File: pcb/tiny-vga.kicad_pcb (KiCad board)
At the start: 2 copper layers, 40 x 33 mm, 15 parts, among them J1 PMOD, J2 VGA, U1 74LVC245A

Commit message: Update parts for aisler
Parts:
- removed C1: C, Capacitor_SMD:C_0603_1608Metric_Pad1.08x0.95mm_HandSolder
- removed JP1: SolderJumper_3_Bridged12, Jumper:SolderJumper-3_P1.3mm_Bridged2Bar12_RoundedPad1.0x1.5mm
- RN1, RN2, RN3: footprint Resistor_SMD:R_Array_Convex_4x0402 -> Resistor_SMD:R_Array_Convex_4x0603
- U1: value 74LVC245A -> 74LVC245APW,118
- moved REF** 24.6 mm to (130.5, 64.6)
- moved RN1 0.60 mm to (153.1, 79.3)
- moved RN2 0.60 mm to (153.1, 83.5)
- moved RN3 0.60 mm to (153.1, 87.5)
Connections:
- U1 pad 1: Net-(JP1-C) -> GND
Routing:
- net +3.3V: track 19.8 -> 13.3 mm
- net Net-(JP1-C): track 4.40 -> 0.00 mm
- net GND: track 16.6 -> 15.1 mm, vias 7 -> 6
- net G0: track 6.72 -> 8.03 mm
- net B0: track 8.12 -> 9.20 mm
- net Net-(RN2A-R1.2): track 2.34 -> 3.34 mm
- net Net-(RN1A-R1.2): track 2.56 -> 3.50 mm
- net R0: track 7.11 -> 7.93 mm
- net Net-(RN3A-R1.2): track 2.95 -> 3.48 mm

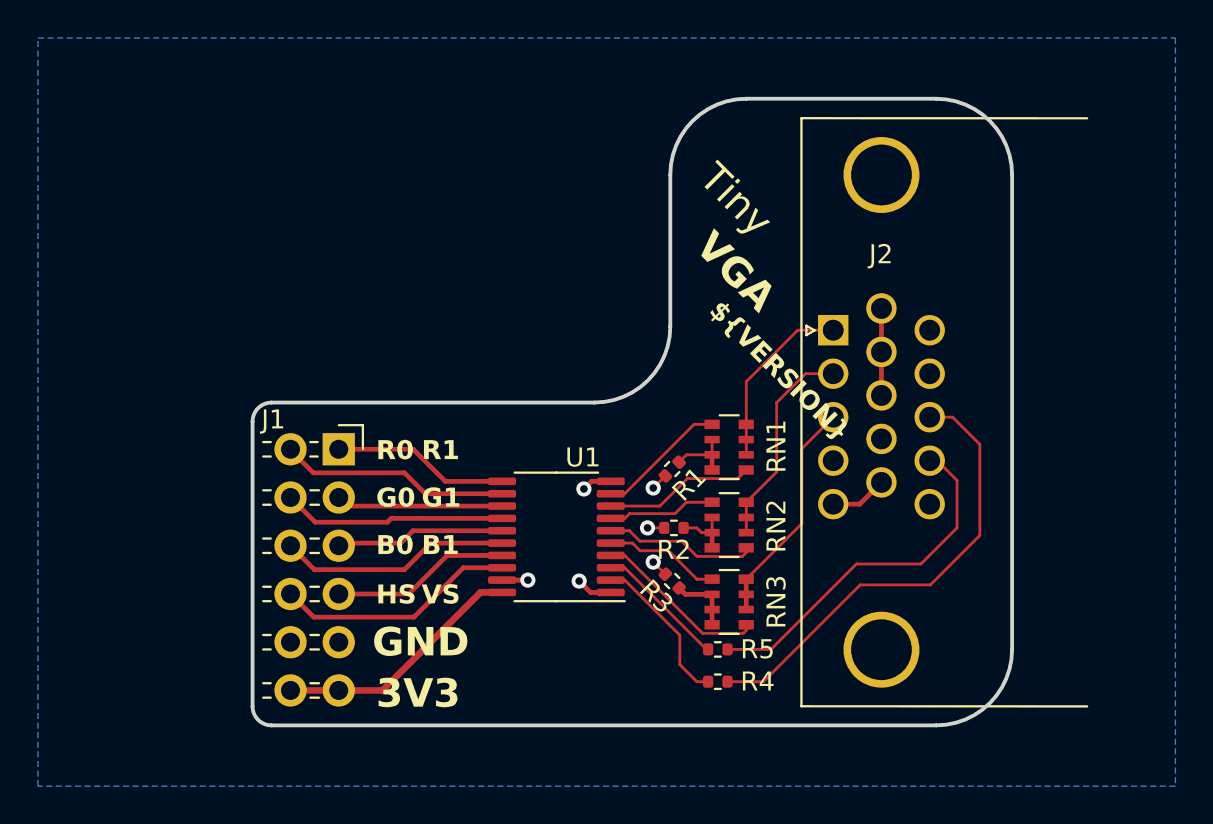
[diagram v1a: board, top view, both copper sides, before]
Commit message: Add AISLER support
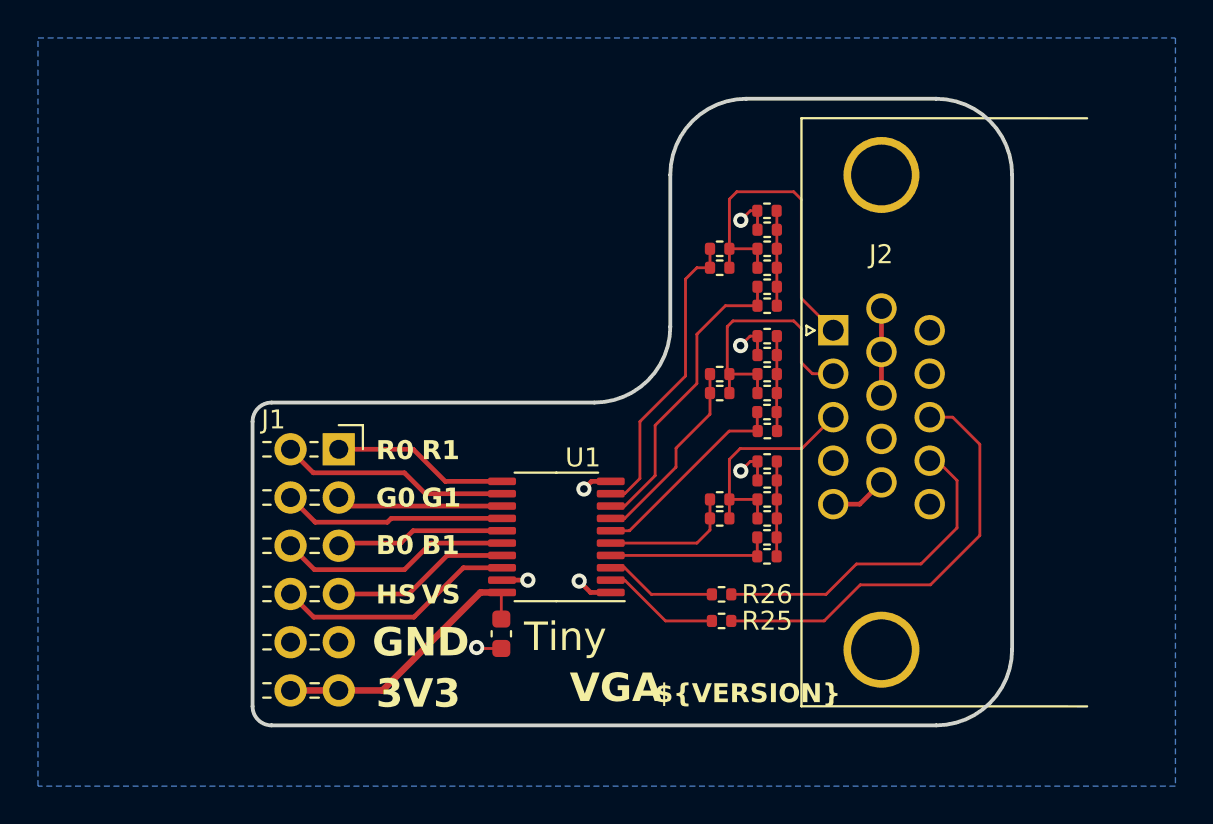
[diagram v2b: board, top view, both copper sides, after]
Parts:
- removed RN1, RN2, RN3: 360R, Resistor_SMD:R_Array_Convex_4x0603
- added C1: 100n, Capacitor_SMD:C_0603_1608Metric, F.Cu at (141.1, 89.2)
- added R10: 1.5k, Resistor_SMD:R_0402_1005Metric, F.Cu at (155.1, 74.5)
- added R11: 470, Resistor_SMD:R_0402_1005Metric, F.Cu at (152.6, 76.5)
- added R12: 220R, Resistor_SMD:R_0402_1005Metric, F.Cu at (155.1, 75.5)
- added R13: 1.5k, Resistor_SMD:R_0402_1005Metric, F.Cu at (152.6, 75.5)
- added R14: 1k, Resistor_SMD:R_0402_1005Metric, F.Cu at (155.1, 76.5)
- added R15: 1.5k, Resistor_SMD:R_0402_1005Metric, F.Cu at (155.1, 77.5)
- added R16: 470, Resistor_SMD:R_0402_1005Metric, F.Cu at (155.1, 78.5)
- added R17: 470, Resistor_SMD:R_0402_1005Metric, F.Cu at (155.1, 80.1)
- added R18: 1.5k, Resistor_SMD:R_0402_1005Metric, F.Cu at (155.1, 81.1)
- added R19: 470, Resistor_SMD:R_0402_1005Metric, F.Cu at (152.6, 82.1)
- added R20: 220R, Resistor_SMD:R_0402_1005Metric, F.Cu at (155.1, 82.1)
- added R21: 1.5k, Resistor_SMD:R_0402_1005Metric, F.Cu at (152.6, 83.1)
- added R22: 1k, Resistor_SMD:R_0402_1005Metric, F.Cu at (155.1, 83.1)
- added R23: 1.5k, Resistor_SMD:R_0402_1005Metric, F.Cu at (155.1, 84.1)
- added R24: 470, Resistor_SMD:R_0402_1005Metric, F.Cu at (155.1, 85.1)
- added R25: 49.9R, Resistor_SMD:R_0402_1005Metric, F.Cu at (152.7, 88.5)
- added R26: 49.9R, Resistor_SMD:R_0402_1005Metric, F.Cu at (152.7, 87.1)
- added R6: 1k, Resistor_SMD:R_0402_1005Metric, F.Cu at (155.1, 69.9)
- added R7: 1.5k, Resistor_SMD:R_0402_1005Metric, F.Cu at (155.1, 70.9)
- added R8: 470, Resistor_SMD:R_0402_1005Metric, F.Cu at (155.1, 71.9)
- added R9: 470, Resistor_SMD:R_0402_1005Metric, F.Cu at (155.1, 73.5)
- R1, R3: value 360R -> 470
- R2: value 360R -> 1.5k
- R4: value 47R -> 220R
- R5: value 47R -> 1.5k
- moved REF** 25.1 mm to (155.3, 68.7)
- moved R4 22.9 mm to (155.1, 68.9), turned to 180 degrees
- moved R5 20.1 mm to (152.6, 69.9)
- moved R3 17.7 mm to (152.6, 68.9), turned to 0 degrees
- moved R2 16.4 mm to (155.1, 67.9)
- moved R1 14.5 mm to (155.1, 66.9), turned to 180 degrees
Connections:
- R1 pad 1: Net-(RN1A-R1.2) -> Net-(R1-Pad1)
- R2 pad 1: Net-(RN2A-R1.2) -> Net-(R1-Pad1)
- R3 pad 1: Net-(RN3A-R1.2) -> R1
- R3 pad 2: GND -> AnalogR
- R4 pad 1: Hsync -> Net-(R1-Pad1)
- R4 pad 2: Net-(J2-Pad13) -> AnalogR
- R5 pad 1: Vsync -> R1
- R5 pad 2: Net-(J2-Pad14) -> AnalogR
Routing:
- net R1: track 6.85 -> 15.9 mm
- net R0: track 7.93 -> 16.2 mm
- net AnalogR: track 9.55 -> 17.8 mm
- net Net-(R10-Pad1): track 0.00 -> 5.01 mm
- net Net-(R1-Pad1): track 0.00 -> 5.00 mm
- net Net-(R17-Pad1): track 0.00 -> 5.00 mm
- net GND: track 15.1 -> 20.0 mm, vias 6 -> 7
- net G1: track 5.69 -> 10.2 mm
- net Net-(RN1A-R1.2): track 3.50 -> 0.00 mm
- net Net-(RN3A-R1.2): track 3.48 -> 0.00 mm
- net Net-(RN2A-R1.2): track 3.34 -> 0.00 mm
- net G0: track 8.03 -> 10.9 mm
- net AnalogG: track 11.1 -> 13.9 mm
- net Hsync: track 8.25 -> 6.22 mm
- net Net-(J2-Pad13): track 24.5 -> 23.0 mm
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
